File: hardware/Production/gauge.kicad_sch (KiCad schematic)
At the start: 66 parts, among them J102 Cell 1 NTC wires, J105 Cell 2 NTC wires, J106 Cell 3 NTC wires, J107 Cell 4 NTC wires, J108 PACK-, J109 CELL1 tap, J110 CELL2 tap, J111 CELL3 tap, J112 PACK+, J113 LOAD PACK_P, J114 LOAD GND, Q101 AGM404AP1, Q102 AGM404AP1, Q103 AO3400A, Q104 AO3400A, U101 BQ40Z50RSMR-R2, U102 BQ294700DSGR

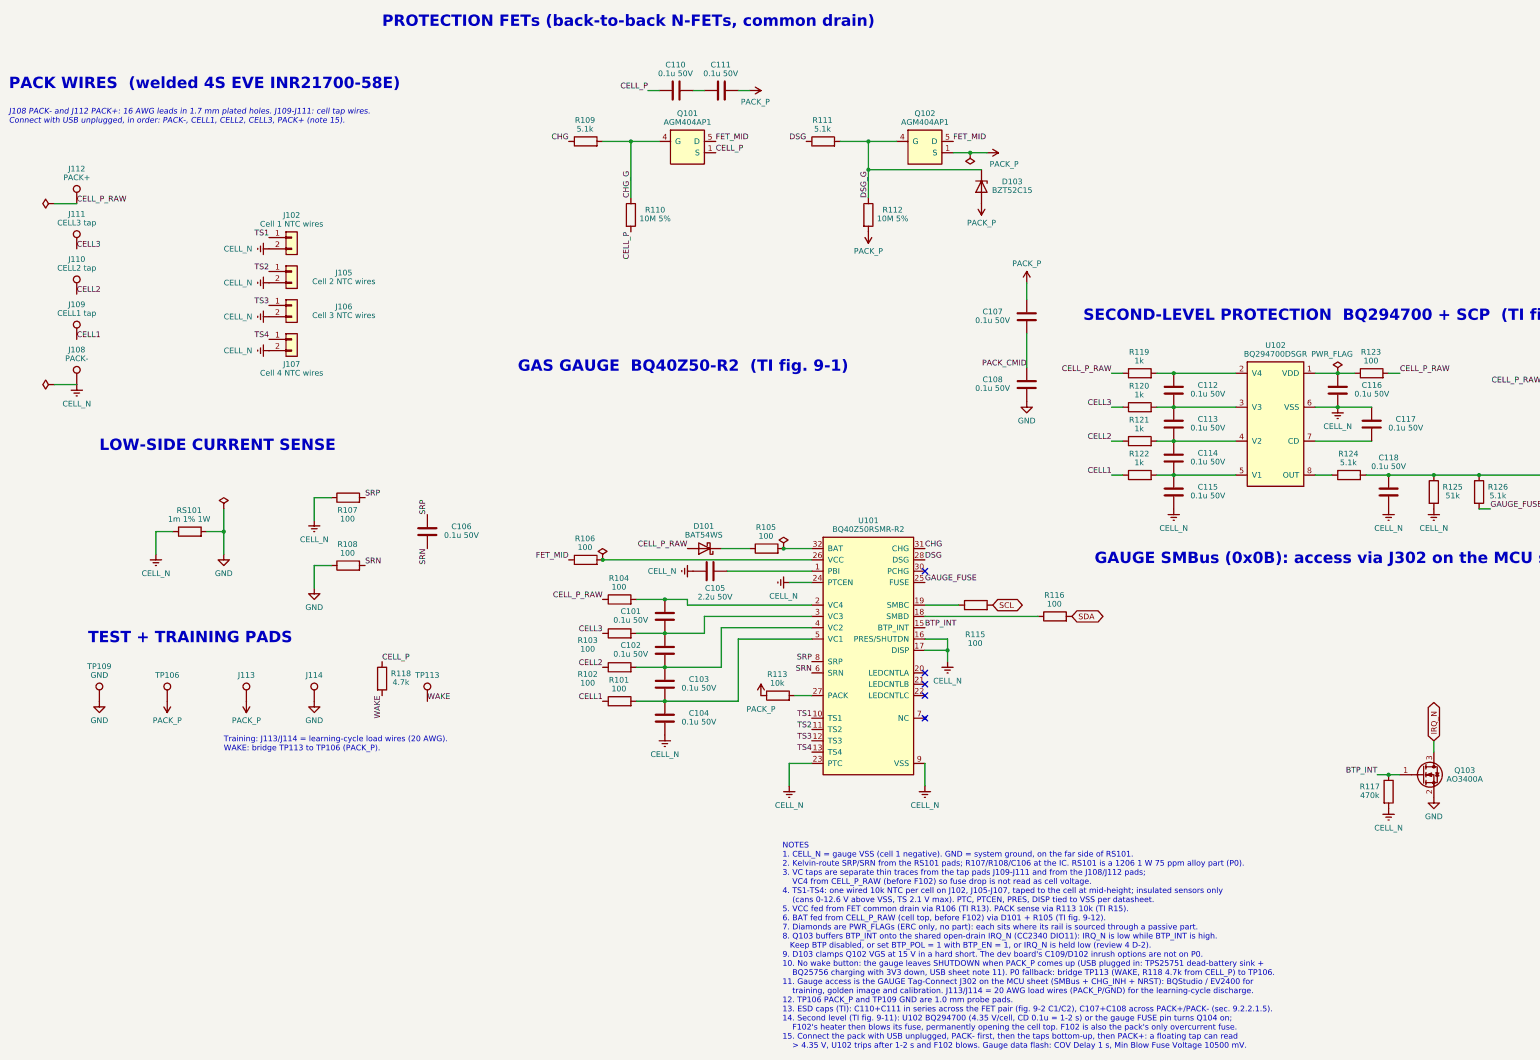
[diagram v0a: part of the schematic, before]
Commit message: Production board: tail slots, 1N/4P Kelvin nets, carrier peg holes, cup keep-outs
Schematic (make_production.py, regenerated):
- J108-J112 become plated slots for the nickel tails; J115 (1N) and J116 (4P)
  are the Kelvin fingers on new nets CELL_1N / CELL_4P (SLUA660 2.3-2.4).
  CELL_1N: gauge VSS star, U102 VSS, decoupling, NTC returns. CELL_4P: VC4,
  U102 V4/VDD, D101. Shunt, SRP and Q104 stay on CELL_N; F102 on CELL_P_RAW.
- H101-H104: cover standoffs -> 2.2 mm NPTH carrier peg holes.
- R413/R513 11.8k and the ICHG heading now come from the generator.
- Symbol uuids are kept across regens so Update PCB keeps placed parts.
- check_netlist accepts "new NAME" net moves; tidy notes updated.

Board: cup keep-outs (rails split at the filler, gap filler, tail runs,
vent, antenna, top stops), footprints swapped and nets applied from the
schematic (checked pad by pad), slots and pegs placed and locked.

make_board.py: --keepouts writes zones as text (KiCad 10 python can't build
outlines), --mech replaces --standoffs and keeps the .kicad_pro.
monolith_shell.py holds the cup's board-facing values (CUP_*, cup_rails).
Docs: README sections, p0-assembly solder order and Kelvin wording.

Co-Authored-By: Claude Opus 5.5 <noreply@anthropic.com>
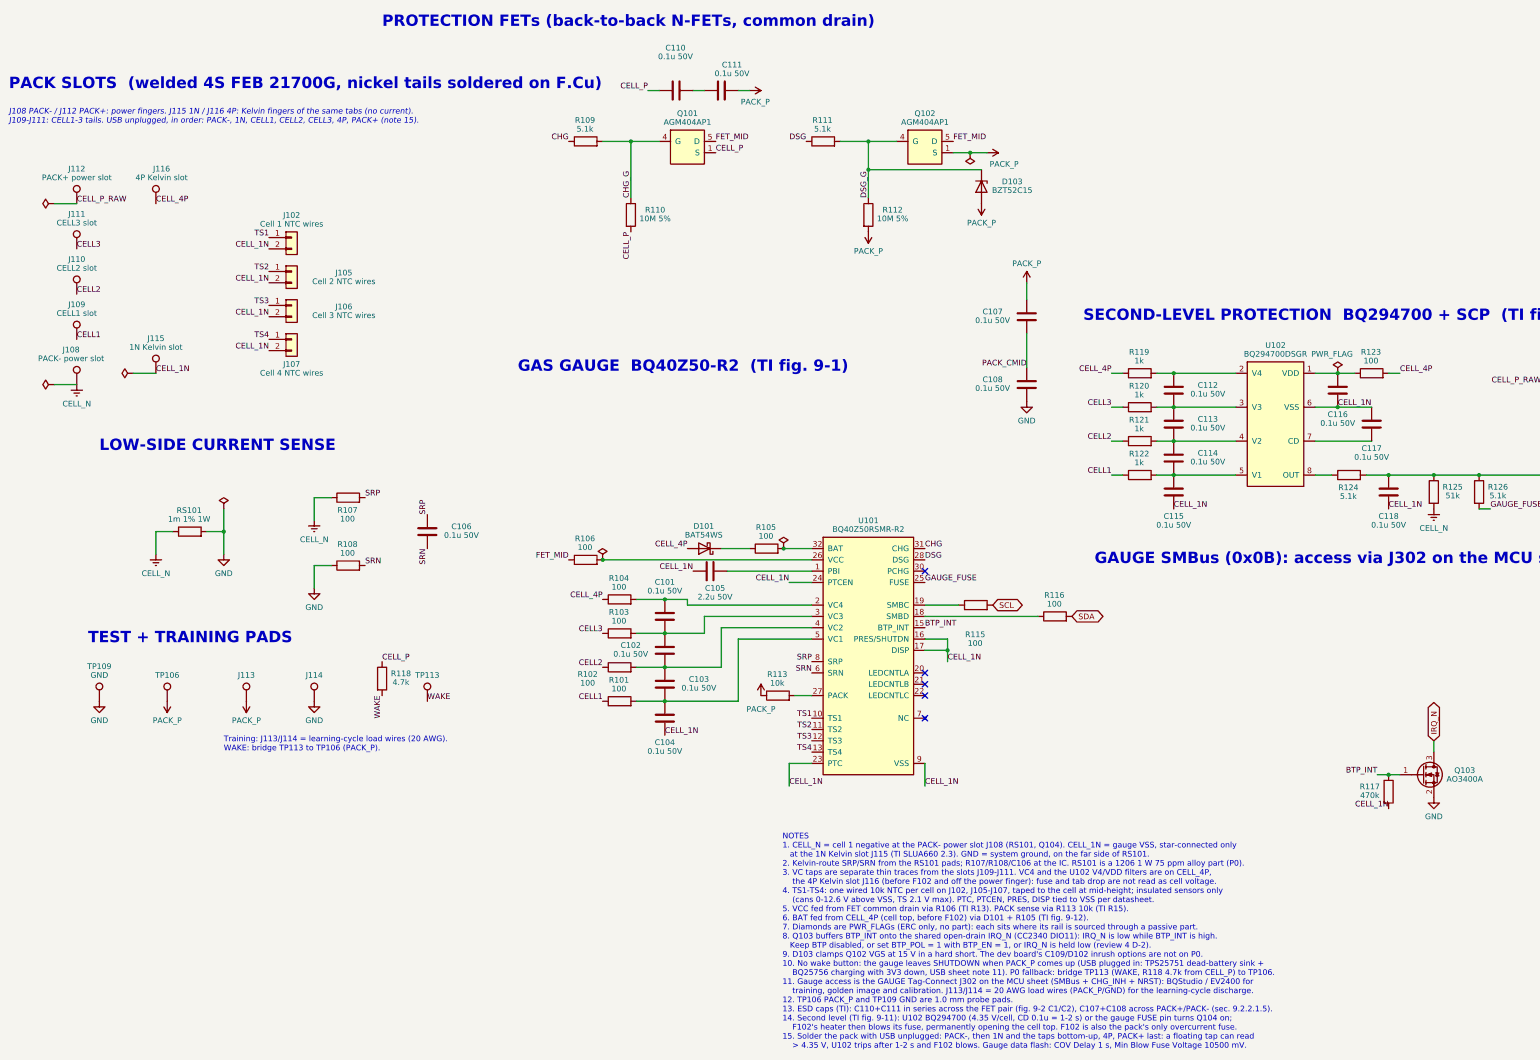
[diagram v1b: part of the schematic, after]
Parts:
- added J115: 1N Kelvin slot, MonolithDev:Slot_Tab_1.6x0.6mm, symbol Connector:TestPoint
- added J116: 4P Kelvin slot, MonolithDev:Slot_Tab_1.6x0.6mm, symbol Connector:TestPoint
- J108: value PACK- -> PACK- power slot; footprint Connector_Wire:SolderWire-1.5sqmm_1x01_D1.7mm_OD3.9mm -> MonolithDev:Slot_Tab_4.6x0.6mm; Notes CELL_N -> (none)
- J109: value CELL1 tap -> CELL1 slot; footprint Connector_Wire:SolderWire-0.15sqmm_1x01_D0.5mm_OD1.5mm -> MonolithDev:Slot_Tab_3.4x0.6mm
- J110: value CELL2 tap -> CELL2 slot; footprint Connector_Wire:SolderWire-0.15sqmm_1x01_D0.5mm_OD1.5mm -> MonolithDev:Slot_Tab_3.4x0.6mm
- J111: value CELL3 tap -> CELL3 slot; footprint Connector_Wire:SolderWire-0.15sqmm_1x01_D0.5mm_OD1.5mm -> MonolithDev:Slot_Tab_3.4x0.6mm
- J112: value PACK+ -> PACK+ power slot; footprint Connector_Wire:SolderWire-1.5sqmm_1x01_D1.7mm_OD3.9mm -> MonolithDev:Slot_Tab_4.6x0.6mm; Notes CELL_P_RAW -> (none)
- U102: Notes Independent of the gauge: 4.35 V/cell OVP (hysteresis 0.30 V), active-high OUT (~7 V) after the CD delay. RIN must be 1k (device calibrated with it). Exposed pad to VSS (CELL_N). -> Independent of the gauge: 4.35 V/cell OVP (hysteresis 0.30 V), active-high OUT (~7 V) after the CD delay. RIN must be 1k (device calibrated with it). Exposed pad to VSS (CELL_1N, the Kelvin ground at the 1N tab).
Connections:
- net CELL_N: no longer C104.2, C105.2, C115.2, C116.2, C117.1, C118.2, J102.2 (Pin_2), J105.2 (Pin_2), J106.2 (Pin_2), J107.2 (Pin_2), R117.2, U101.16 (PRES/SHUTDN), U101.17 (DISP), U101.23 (PTC), U101.24 (PTCEN), U101.33 (VSS), U101.9 (VSS), U102.6 (VSS), U102.9 (VSS)
- net CELL_P_RAW: no longer D101.2 (A), R104.1, R119.1, R123.2
- new net CELL_1N: C104.2, C105.2, C115.2, C116.2, C117.1, C118.2, J102.2 (Pin_2), J105.2 (Pin_2), J106.2 (Pin_2), J107.2 (Pin_2), J115.1, R117.2, U101.16 (PRES/SHUTDN), U101.17 (DISP), U101.23 (PTC), U101.24 (PTCEN), U101.33 (VSS), U101.9 (VSS), U102.6 (VSS), U102.9 (VSS)
- new net CELL_4P: D101.2 (A), J116.1, R104.1, R119.1, R123.2
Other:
- note added: "J108 PACK- / J112 PACK+: power fingers. J115 1N / J116 4P: Kelvin fingers of the same tabs (no current). J109-J111: CELL1-3 tails. USB unplugged, in order: PACK-, 1N, CELL1, CELL2, CELL3, 4P, PACK+ (note 15)."
- note added: "NOTES 1. CELL_N = cell 1 negative at the PACK- power slot J108 (RS101, Q104). CELL_1N = gauge VSS, star-connected only at the 1N Kelvin slot J115 (TI SLUA660 2.3). GND = system ground, on the far side of RS101. 2. Kelvin-route SRP/SRN from the RS101 pads; R107/R108/C106 at the IC. RS101 is a 1206 1 W 75 ppm alloy part (P0). 3. VC taps are separate thin traces from the slots J109-J111. VC4 and the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"
- note added: "PACK SLOTS (welded 4S FEB 21700G, nickel tails soldered on F.Cu)"
- note removed: "J108 PACK- and J112 PACK+: 16 AWG leads in 1.7 mm plated holes. J109-J111: cell tap wires. Connect with USB unplugged, in order: PACK-, CELL1, CELL2, CELL3, PACK+ (note 15)."
- note removed: "NOTES 1. CELL_N = gauge VSS (cell 1 negative). GND = system ground, on the far side of RS101. 2. Kelvin-route SRP/SRN from the RS101 pads; R107/R108/C106 at the IC. RS101 is a 1206 1 W 75 ppm alloy part (P0). 3. VC taps are separate thin traces from the tap pads J109-J111 and from the J108/J112 pads; VC4 from CELL_P_RAW (before F102) so fuse drop is not read as cell voltage. 4. TS1-TS4: one wired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"
- note removed: "PACK WIRES (welded 4S EVE INR21700-58E)"

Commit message: Production board: PACK wire holes for the option C wire tails
J108 / J112 go from the 4.6 mm PACK power slots to Ø1.5 mm plated holes
(0.4 mm ring) for the 18 AWG thin-wall PTFE power wires, at sb_pack_holes():
KiCad (86.975, 135.7255) and (113.025, 135.7255), F.Cu, locked. The Kelvin
wires stay in the J115 / J116 slots.

- make_production.py: WIRE_FP footprint generated from SB_PWIRE_*, used for
  J108 / J112; SLOT_REFS keeps the five slots, WIRE_REFS the two holes.
- make_board.py: --mech also places the wire holes; keepout_list() follows
  the merged model (three tail runs, four KO_B_wire_* from sb_wire_runs()).
- Board: J108 / J112 swapped and placed as Update PCB + --mech would; the four
  PACK / Kelvin finger tail keep-outs replaced by KO_B_wire_*. Other
  keep-outs untouched (KO_F_above_antenna stays removed).
- Schematic Footprint / Value fields and sheet notes; Slot_Tab_4.6x0.6mm
  dropped from the library; README, spec and assembly docs.

KiCad is not available in this environment, so DRC has not been run; a
script check covers the outline, edge rule, ring and courtyards.

Co-Authored-By: Claude Opus 5.5 (1M context) <noreply@anthropic.com>
Claude-Session: https://claude.ai/code/session_01VT5ZsG8mLjRjzAJFn7LJRo
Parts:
- J108: value PACK- power slot -> PACK- power wire; footprint MonolithDev:Slot_Tab_4.6x0.6mm -> MonolithDev:SolderWire-18AWG_PTFE_1x01_D1.5mm_OD2.3mm
- J112: value PACK+ power slot -> PACK+ power wire; footprint MonolithDev:Slot_Tab_4.6x0.6mm -> MonolithDev:SolderWire-18AWG_PTFE_1x01_D1.5mm_OD2.3mm
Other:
- note added: "J108 PACK- / J112 PACK+: 18 AWG power wires in 1.5 mm holes. J115 1N / J116 4P: Kelvin wires from the same pads. J109-J111: CELL1-3 tails. USB unplugged, in order: PACK-, 1N, CELL1, CELL2, CELL3, 4P, PACK+ (note 15)."
- note added: "NOTES 1. CELL_N = cell 1 negative at the PACK- power wire J108 (RS101, Q104). CELL_1N = gauge VSS, star-connected only at the 1N Kelvin slot J115 (TI SLUA660 2.3). GND = system ground, on the far side of RS101. 2. Kelvin-route SRP/SRN from the RS101 pads; R107/R108/C106 at the IC. RS101 is a 1206 1 W 75 ppm alloy part (P0). 3. VC taps are separate thin traces from the slots J109-J111. VC4 and the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"
- note added: "PACK SLOTS + WIRES (welded 4S BAK 65E, tails and wires soldered on F.Cu)"
- note removed: "J108 PACK- / J112 PACK+: power fingers. J115 1N / J116 4P: Kelvin fingers of the same tabs (no current). J109-J111: CELL1-3 tails. USB unplugged, in order: PACK-, 1N, CELL1, CELL2, CELL3, 4P, PACK+ (note 15)."
- note removed: "NOTES 1. CELL_N = cell 1 negative at the PACK- power slot J108 (RS101, Q104). CELL_1N = gauge VSS, star-connected only at the 1N Kelvin slot J115 (TI SLUA660 2.3). GND = system ground, on the far side of RS101. 2. Kelvin-route SRP/SRN from the RS101 pads; R107/R108/C106 at the IC. RS101 is a 1206 1 W 75 ppm alloy part (P0). 3. VC taps are separate thin traces from the slots J109-J111. VC4 and the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"
- note removed: "PACK SLOTS (welded 4S FEB 21700G, nickel tails soldered on F.Cu)"
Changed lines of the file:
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@@
 		)
 	)
-	(text "PACK SLOTS  (welded 4S FEB 21700G, nickel tails soldered on F.Cu)"
+	(text "PACK SLOTS + WIRES  (welded 4S BAK 65E, tails and wires soldered on F.Cu)"
 		(exclude_from_sim no)
 		(at 22.86 33.02 0)
@@
 		)
 	)
-	(text "NOTES\n1. CELL_N = cell 1 negative at the PACK- power slot J108 (RS101, Q104). CELL_1N = gauge VSS, star-connected only\n   at the 1N Kelvin slot J115 (TI SLUA660 2.3). GND = system ground, on the far side of RS101.\n2. Kelvin-route SRP/SRN from the RS101 pads; R107/R108/C106 at the IC. RS101 is a 1206 1 W 75 ppm alloy part (P0).\n3. VC taps are separate thin traces from the slots J109-J111. VC4 and the U102 V4/VDD filters are on CELL_4P,\n    the 4P Kelvin slot J116 (before F102 and off the power finger): fuse and tab drop are not read as cell voltage.\n4. TS1-TS4: one wired 10k NTC per cell on J102, J105-J107, taped to the cell at mid-height; insulated sensors only\n    (cans 0-12.6 V above VSS, TS 2.1 V max). PTC, PTCEN, PRES, DISP tied to VSS per datasheet.\n5. VCC fed from FET common drain via R106 (TI R13). PACK sense via R113 10k (TI R15).\n6. BAT fed from CELL_4P (cell top, before F102) via D101 + R105 (TI fig. 9-12).\n7. Diamonds are PWR_FLAGs (ERC only, no part): each sits where its rail is sourced through a passive part.\n8. Q103 buffers BTP_INT onto the shared open-drain IRQ_N (CC2340 DIO11): IRQ_N is low while BTP_INT is high.\n   Keep BTP disabled, or set BTP_POL = 1 with BTP_EN = 1, or IRQ_N is held low (review 4 D-2).\n9. D103 clamps Q102 VGS at 15 V in a hard short. The dev board's C109/D102 inrush options are not on P0.\n10. No wake button: the gauge leaves SHUTDOWN when PACK_P comes up (USB plugged in: TPS25751 dead-battery sink +\n    BQ25756 charging with 3V3 down, USB sheet note 11). P0 fallback: bridge TP113 (WAKE, R118 4.7k from CELL_P) to TP106.\n11. Gauge access is the GAUGE Tag-Connect J302 on the MCU sheet (SMBus + CHG_INH + NRST): BQStudio / EV2400 for\n    training, golden image and calibration. J113/J114 = 20 AWG load wires (PACK_P/GND) for the learning-cycle discharge.\n12. TP106 PACK_P and TP109 GND are 1.0 mm probe pads.\n13. ESD caps (TI): C110+C111 in series across the FET pair (fig. 9-2 C1/C2), C107+C108 across PACK+/PACK- (sec. 9.2.2.1.5).\n14. Second level (TI fig. 9-11): U102 BQ294700 (4.35 V/cell, CD 0.1u = 1-2 s) or the gauge FUSE pin turns Q104 on;\n    F102's heater then blows its fuse, permanently opening the cell top. F102 is also the pack's only overcurrent fuse.\n15. Solder the pack with USB unplugged: PACK-, then 1N and the taps bottom-up, 4P, PACK+ last: a floating tap can read\n    > 4.35 V, U102 trips after 1-2 s and F102 blows. Gauge data flash: COV Delay 1 s, Min Blow Fuse Voltage 10500 mV."
+	(text "NOTES\n1. CELL_N = cell 1 negative at the PACK- power wire J108 (RS101, Q104). CELL_1N = gauge VSS, star-connected only\n   at the 1N Kelvin slot J115 (TI SLUA660 2.3). GND = system ground, on the far side of RS101.\n2. Kelvin-route SRP/SRN from the RS101 pads; R107/R108/C106 at the IC. RS101 is a 1206 1 W 75 ppm alloy part (P0).\n3. VC taps are separate thin traces from the slots J109-J111. VC4 and the U102 V4/VDD filters are on CELL_4P,\n    the 4P Kelvin slot J116 (before F102 and off the power wire): fuse and wire drop are not read as cell voltage.\n4. TS1-TS4: one wired 10k NTC per cell on J102, J105-J107, taped to the cell at mid-height; insulated sensors only\n    (cans 0-12.6 V above VSS, TS 2.1 V max). PTC, PTCEN, PRES, DISP tied to VSS per datasheet.\n5. VCC fed from FET common drain via R106 (TI R13). PACK sense via R113 10k (TI R15).\n6. BAT fed from CELL_4P (cell top, before F102) via D101 + R105 (TI fig. 9-12).\n7. Diamonds are PWR_FLAGs (ERC only, no part): each sits where its rail is sourced through a passive part.\n8. Q103 buffers BTP_INT onto the shared open-drain IRQ_N (CC2340 DIO11): IRQ_N is low while BTP_INT is high.\n   Keep BTP disabled, or set BTP_POL = 1 with BTP_EN = 1, or IRQ_N is held low (review 4 D-2).\n9. D103 clamps Q102 VGS at 15 V in a hard short. The dev board's C109/D102 inrush options are not on P0.\n10. No wake button: the gauge leaves SHUTDOWN when PACK_P comes up (USB plugged in: TPS25751 dead-battery sink +\n    BQ25756 charging with 3V3 down, USB sheet note 11). P0 fallback: bridge TP113 (WAKE, R118 4.7k from CELL_P) to TP106.\n11. Gauge access is the GAUGE Tag-Connect J302 on the MCU sheet (SMBus + CHG_INH + NRST): BQStudio / EV2400 for\n    training, golden image and calibration. J113/J114 = 20 AWG load wires (PACK_P/GND) for the learning-cycle discharge.\n12. TP106 PACK_P and TP109 GND are 1.0 mm probe pads.\n13. ESD caps (TI): C110+C111 in series across the FET pair (fig. 9-2 C1/C2), C107+C108 across PACK+/PACK- (sec. 9.2.2.1.5).\n14. Second level (TI fig. 9-11): U102 BQ294700 (4.35 V/cell, CD 0.1u = 1-2 s) or the gauge FUSE pin turns Q104 on;\n    F102's heater then blows its fuse, permanently opening the cell top. F102 is also the pack's only overcurrent fuse.\n15. Solder the pack with USB unplugged: PACK-, then 1N and the taps bottom-up, 4P, PACK+ last: a floating tap can read\n    > 4.35 V, U102 trips after 1-2 s and F102 blows. Gauge data flash: COV Delay 1 s, Min Blow Fuse Voltage 10500 mV."
 		(exclude_from_sim no)
 		(at 196.596 248.412 0)
@@
 		)
 	)
-	(text "J108 PACK- / J112 PACK+: power fingers. J115 1N / J116 4P: Kelvin fingers of the same tabs (no current).\nJ109-J111: CELL1-3 tails. USB unplugged, in order: PACK-, 1N, CELL1, CELL2, CELL3, 4P, PACK+ (note 15)."
+	(text "J108 PACK- / J112 PACK+: 18 AWG power wires in 1.5 mm holes. J115 1N / J116 4P: Kelvin wires from the same pads.\nJ109-J111: CELL1-3 tails. USB unplugged, in order: PACK-, 1N, CELL1, CELL2, CELL3, 4P, PACK+ (note 15)."
 		(exclude_from_sim no)
 		(at 22.86 40.64 0)
@@
 			)
 		)
-		(property "Value" "PACK- power slot"
+		(property "Value" "PACK- power wire"
 			(at 36.83 93.21 0)
 			(show_name no)
@@
 			)
 		)
-		(property "Footprint" "MonolithDev:Slot_Tab_4.6x0.6mm"
+		(property "Footprint" "MonolithDev:SolderWire-18AWG_PTFE_1x01_D1.5mm_OD2.3mm"
 			(at 43.18 99.06 0)
 			(hide yes)
@@
 			)
 		)
-		(property "Value" "PACK+ power slot"
+		(property "Value" "PACK+ power wire"
 			(at 38.10 52.57 0)
 			(show_name no)
@@
 			)
 		)
-		(property "Footprint" "MonolithDev:Slot_Tab_4.6x0.6mm"
+		(property "Footprint" "MonolithDev:SolderWire-18AWG_PTFE_1x01_D1.5mm_OD2.3mm"
 			(at 43.18 58.42 0)
 			(hide yes)
